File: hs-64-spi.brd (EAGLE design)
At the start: 19.3 x 19 mm, 25 parts, among them J1 DF40C-70DP-0.4V(51), J2 A79622-001, U1 RHD2064_BGA, U2 ADXL335_IDAX

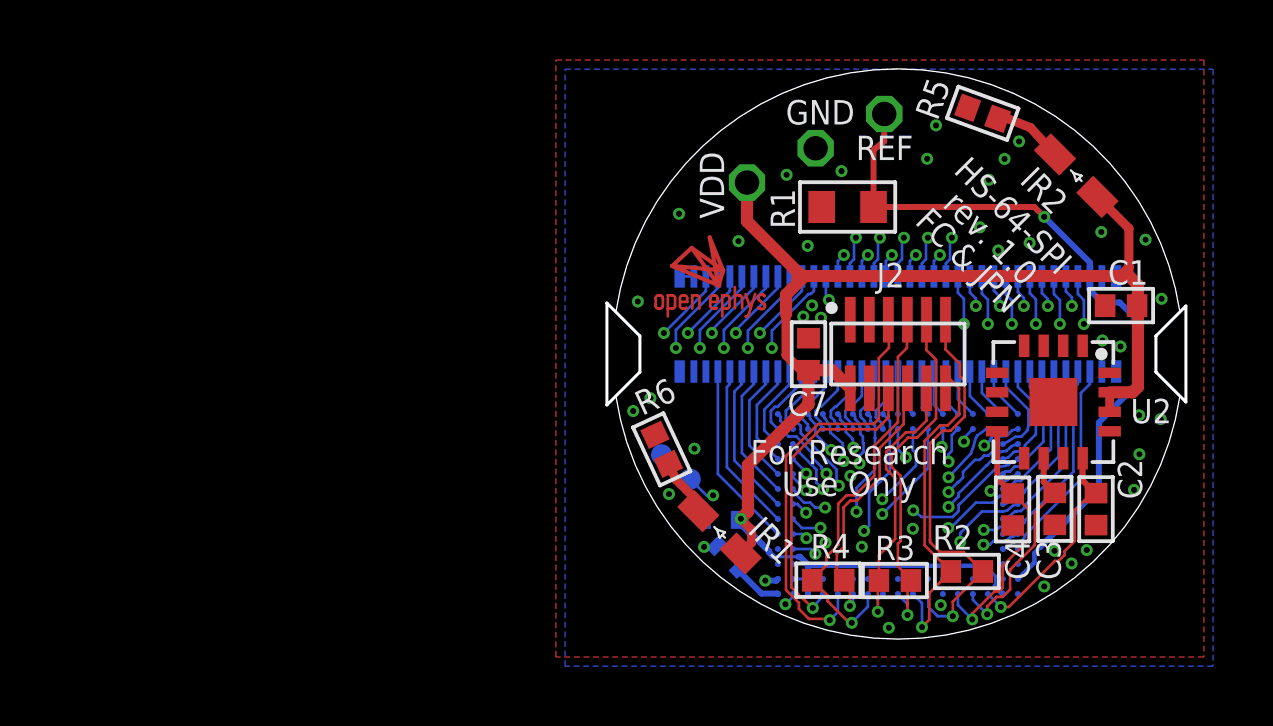
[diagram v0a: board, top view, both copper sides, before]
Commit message: Added PCB design files for the new version 1.1.
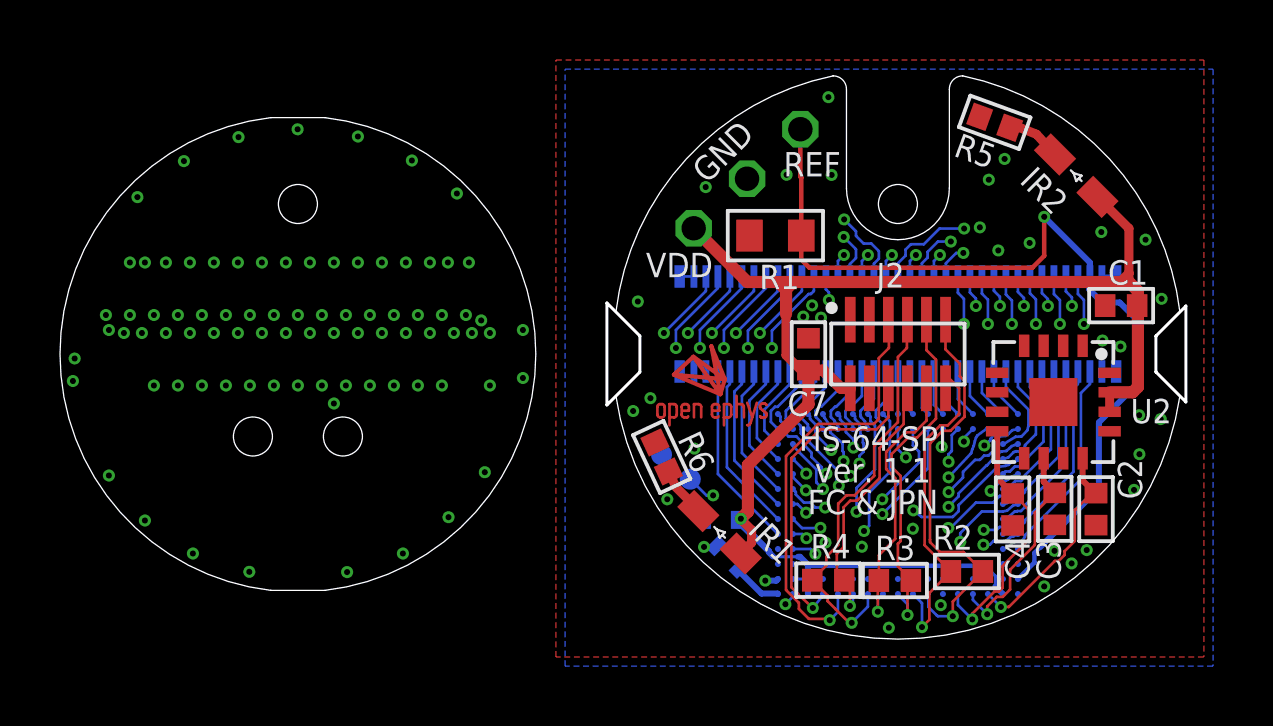
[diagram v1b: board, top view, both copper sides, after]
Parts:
- R5, R6: value 100 -> 820
- moved X 3.63 mm to (-6.37, -1.44)
- moved REF 2.84 mm to (-3.25, 7.49)
- moved R1 2.59 mm to (-4.08, 3.95)
- moved GND 2.50 mm to (-5.03, 5.84)
- moved VDD 2.34 mm to (-6.81, 4.19)
- moved R5 0.50 mm to (3.23, 7.72)
- moved R6 0.25 mm to (-7.87, -3.43)
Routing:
- net REF: track 24.4 -> 29.3 mm
- net E31: track 9.77 -> 13.5 mm
- net E35: track 14.5 -> 16.9 mm
- net +3V3_AN: track 53.4 -> 51.6 mm
- net E27: track 14.7 -> 15.6 mm
- net E23: track 10.5 -> 9.91 mm
- net N$3: track 2.36 -> 1.85 mm
- net AGND: track 0.98 -> 0.92 mm, vias 42 -> 38
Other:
- board size 19.3 x 19 mm -> 37.5 x 18.8 mm
- board text added: "HS-64-SPI ver. 1.1 FC & JPN"
- board text removed: "HS-64-SPI rev. 1.0 FC & JPN"
- board text removed: "www.open-ephys.org"
